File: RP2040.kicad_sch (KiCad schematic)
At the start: 24 parts, among them J1 Conn_01x02, U3 W25Q128JVS, U5 RP2040, Y1 ABM8-272-T3

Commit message: layout rp2040 mwe
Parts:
- J1: now not fitted
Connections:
- no-connect marks 0 -> 1
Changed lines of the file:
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@@
+	)
+	(junction
+		(at 251.46 110.49)
+		(diameter 0)
+		(color 0 0 0 0)
 	)
 	(junction
@@
 	)
 	(junction
-		(at 251.46 110.49)
-		(diameter 0)
-		(color 0 0 0 0)
-	)
-	(junction
 		(at 114.3 194.31)
 		(diameter 0)
 		(color 0 0 0 0)
+	)
+	(no_connect
+		(at 215.9 194.31)
 	)
 	(wire
@@
 				(path "/e63e39d7-6ac0-4ffd-8aa3-1841a4541b55/9c0a3f13-1184-404b-a0f0-9ed0da42fa30"
 					(reference "C7")
-					(unit 1)
-				)
-			)
-		)
-	)
-	(symbol
-		(lib_id "power:+3V3")
-		(at 251.46 110.49 0)
-		(unit 1)
-		(exclude_from_sim no)
-		(in_bom yes)
-		(on_board yes)
-		(dnp no)
-		(property "Reference" "#PWR034"
-			(at 251.46 114.3 0)
-			(effects
-				(font
-					(size 1.27 1.27)
-				)
-				(hide yes)
-			)
-		)
-		(property "Value" "+3V3"
-			(at 251.46 105.41 0)
-			(effects
-				(font
-					(size 1.27 1.27)
-				)
-			)
-		)
-		(property "Footprint" ""
-			(at 251.46 110.49 0)
-			(effects
-				(font
-					(size 1.27 1.27)
-				)
-				(hide yes)
-			)
-		)
-		(property "Datasheet" ""
-			(at 251.46 110.49 0)
-			(effects
-				(font
-					(size 1.27 1.27)
-				)
-				(hide yes)
-			)
-		)
-		(property "Description" ""
-			(at 251.46 110.49 0)
-			(effects
-				(font
-					(size 1.27 1.27)
-				)
-				(hide yes)
-			)
-		)
-		(pin "1"
-		)
-		(instances
-			(project "not-so-fullsize-ortho"
-				(path "/e63e39d7-6ac0-4ffd-8aa3-1841a4541b55/9c0a3f13-1184-404b-a0f0-9ed0da42fa30"
-					(reference "#PWR034")
 					(unit 1)
 				)
@@
 	(symbol
 		(lib_id "power:+3V3")
+		(at 251.46 110.49 0)
+		(unit 1)
+		(exclude_from_sim no)
+		(in_bom yes)
+		(on_board yes)
+		(dnp no)
+		(property "Reference" "#PWR018"
+			(at 251.46 114.3 0)
+			(effects
+				(font
+					(size 1.27 1.27)
+				)
+				(hide yes)
+			)
+		)
+		(property "Value" "+3V3"
+			(at 251.841 106.0958 0)
+			(effects
+				(font
+					(size 1.27 1.27)
+				)
+			)
+		)
+		(property "Footprint" ""
+			(at 251.46 110.49 0)
+			(effects
+				(font
+					(size 1.27 1.27)
+				)
+				(hide yes)
+			)
+		)
+		(property "Datasheet" ""
+			(at 251.46 110.49 0)
+			(effects
+				(font
+					(size 1.27 1.27)
+				)
+				(hide yes)
+			)
+		)
+		(property "Description" ""
+			(at 251.46 110.49 0)
+			(effects
+				(font
+					(size 1.27 1.27)
+				)
+				(hide yes)
+			)
+		)
+		(pin "1"
+		)
+		(instances
+			(project "not-so-fullsize-ortho"
+				(path "/e63e39d7-6ac0-4ffd-8aa3-1841a4541b55/9c0a3f13-1184-404b-a0f0-9ed0da42fa30"
+					(reference "#PWR018")
+					(unit 1)
+				)
+			)
+		)
+	)
+	(symbol
+		(lib_id "power:+3V3")
 		(at 121.92 113.03 0)
 		(unit 1)
@@
 		(in_bom yes)
 		(on_board yes)
-		(dnp no)
+		(dnp yes)
 		(property "Reference" "J1"
 			(at 49.53 134.62 0)

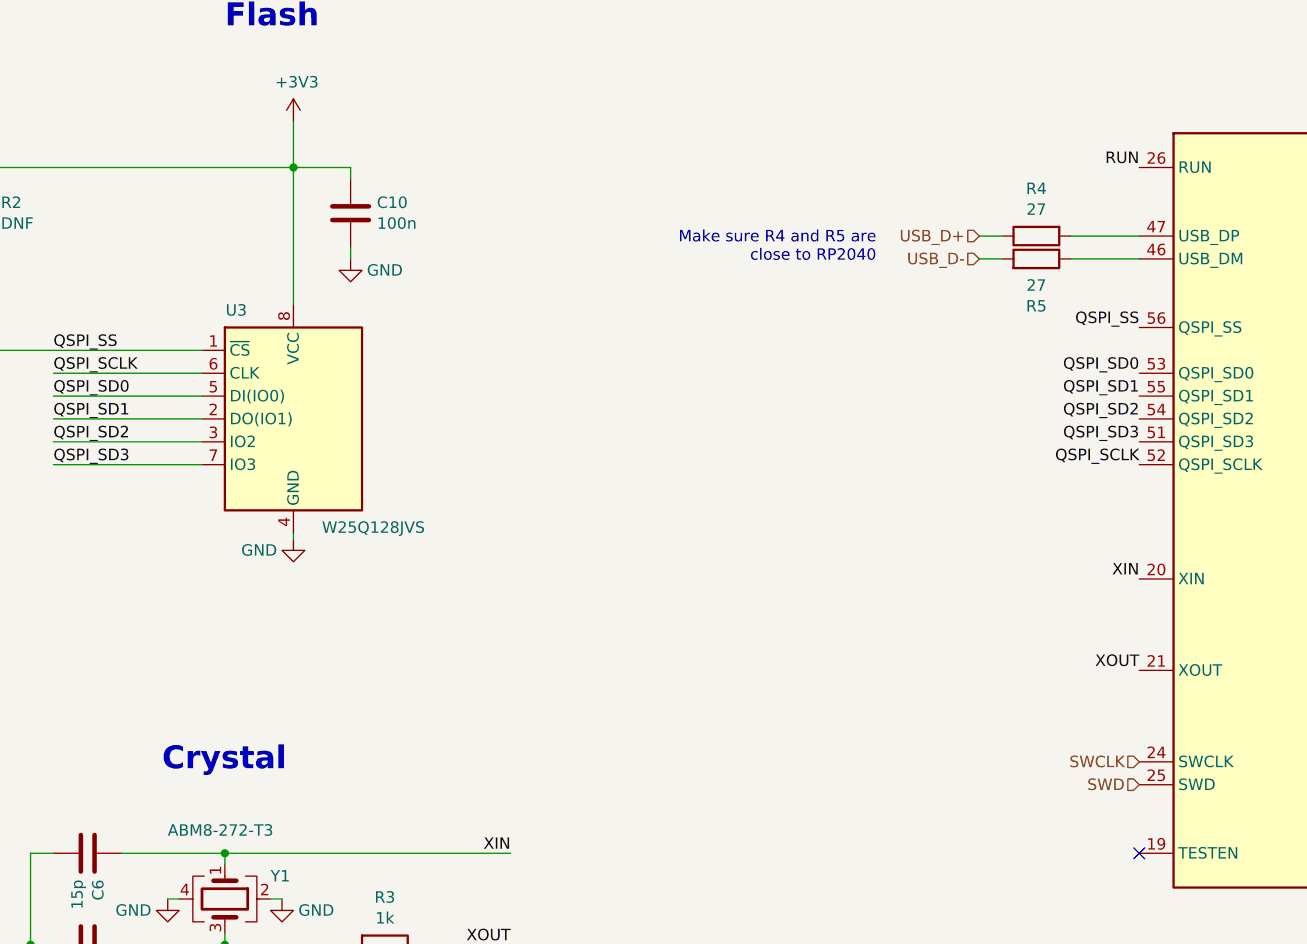
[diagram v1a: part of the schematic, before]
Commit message: routing, rotate leds to make tracks easier
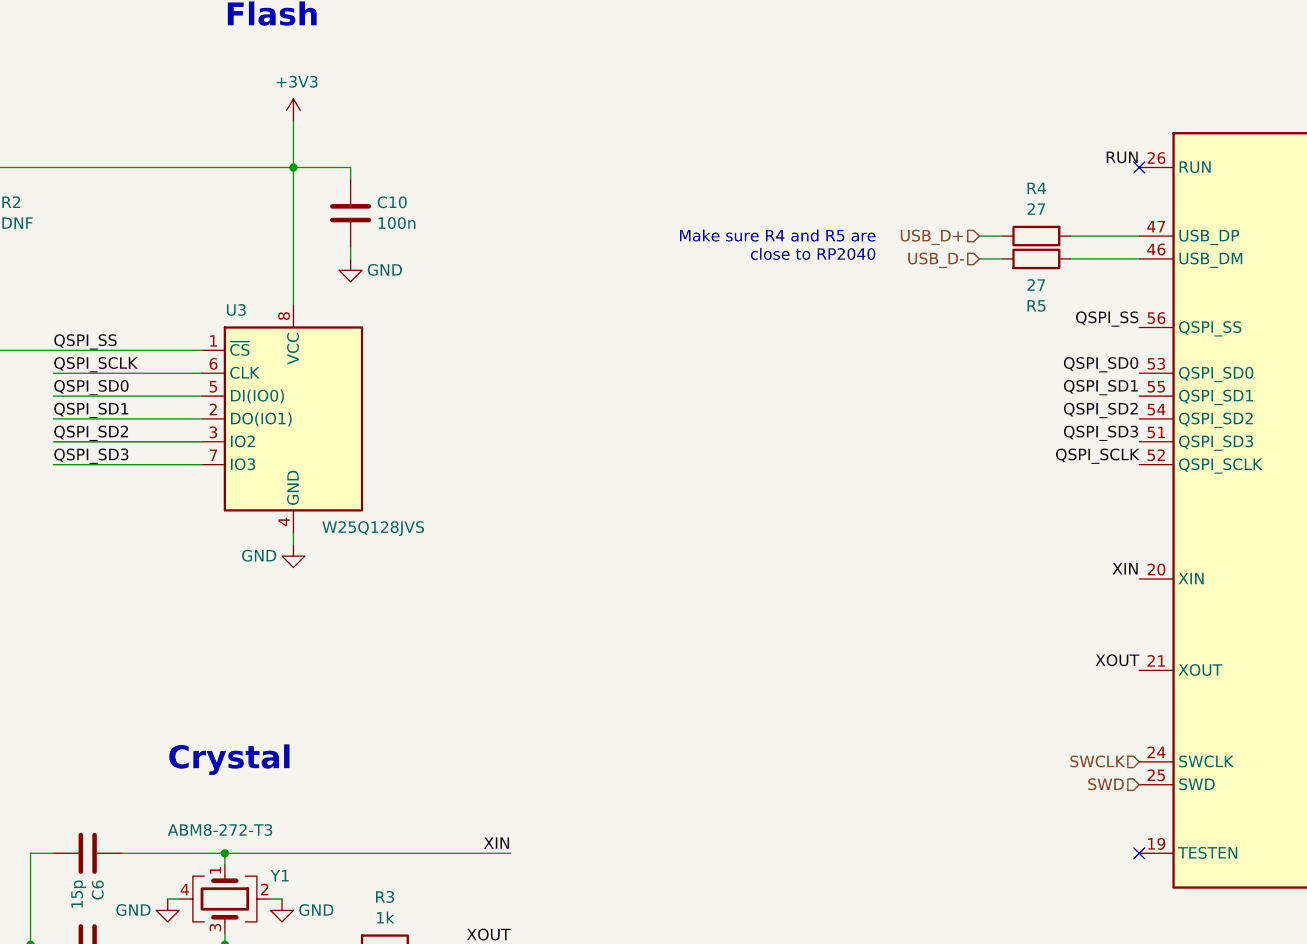
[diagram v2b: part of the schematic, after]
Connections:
- no-connect marks 1 -> 2
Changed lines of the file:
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@@
 		(at 215.9 194.31)
 	)
+	(no_connect
+		(at 215.9 118.11)
+	)
 	(wire
 		(pts
@@
 	(wire
 		(pts
-			(xy 121.92 159.385) (xy 121.92 158.75)
+			(xy 121.92 160.02) (xy 121.92 158.75)
 		)
 		(stroke
@@
 	(text "Crystal"
 		(exclude_from_sim no)
-		(at 107.315 185.42 0)
+		(at 107.95 185.42 0)
 		(effects
 			(font
@@
 			)
 		)
-		(property "Description" ""
+		(property "Description" "Power symbol creates a global label with name \"GND\" , ground"
 			(at 57.15 142.24 0)
 			(effects
@@
 			)
 		)
-		(property "Description" ""
+		(property "Description" "Power symbol creates a global label with name \"+3V3\""
 			(at 389.89 57.15 0)
 			(effects
@@
 			)
 		)
-		(property "Description" ""
+		(property "Description" "Power symbol creates a global label with name \"GND\" , ground"
 			(at 304.8 39.37 0)
 			(effects
@@
 			)
 		)
-		(property "Description" ""
+		(property "Description" "Power symbol creates a global label with name \"+1V1\""
 			(at 332.74 29.21 0)
 			(effects
@@
 			)
 		)
-		(property "Description" ""
+		(property "Description" "Power symbol creates a global label with name \"GND\" , ground"
 			(at 332.74 40.64 0)
 			(effects
@@
 			)
 		)
-		(property "Description" ""
+		(property "Description" "Power symbol creates a global label with name \"+3V3\""
 			(at 251.46 110.49 0)
 			(effects
@@
 			)
 		)
-		(property "Description" ""
+		(property "Description" "Power symbol creates a global label with name \"+3V3\""
 			(at 121.92 113.03 0)
 			(effects
@@
 			)
 		)
-		(property "Description" ""
+		(property "Description" "Power symbol creates a global label with name \"GND\" , ground"
 			(at 107.95 199.39 0)
 			(effects
@@
 			)
 		)
-		(property "Description" ""
+		(property "Description" "Power symbol creates a global label with name \"GND\" , ground"
 			(at 389.89 71.12 0)
 			(effects
@@
 			)
 		)
-		(property "Description" ""
+		(property "Description" "Power symbol creates a global label with name \"GND\" , ground"
 			(at 304.8 68.58 0)
 			(effects
@@
 	(symbol
 		(lib_id "power:GND")
-		(at 121.92 159.385 0)
+		(at 121.92 160.02 0)
 		(unit 1)
 		(exclude_from_sim no)
@@
 		(dnp no)
 		(property "Reference" "#PWR013"
-			(at 121.92 165.735 0)
+			(at 121.92 166.37 0)
 			(effects
 				(font
@@
 		)
 		(property "Value" "GND"
-			(at 118.11 160.655 0)
+			(at 118.11 161.29 0)
 			(effects
 				(font
@@
 		)
 		(property "Footprint" ""
-			(at 121.92 159.385 0)
+			(at 121.92 160.02 0)
 			(effects
 				(font
@@
 		)
 		(property "Datasheet" ""
-			(at 121.92 159.385 0)
+			(at 121.92 160.02 0)
 			(effects
 				(font
@@
 			)
 		)
-		(property "Description" ""
-			(at 121.92 159.385 0)
+		(property "Description" "Power symbol creates a global label with name \"GND\" , ground"
+			(at 121.92 160.02 0)
 			(effects
 				(font
@@
 			)
 		)
-		(property "Description" ""
+		(property "Description" "Power symbol creates a global label with name \"GND\" , ground"
 			(at 389.89 102.87 0)
 			(effects
@@
 			)
 		)
-		(property "Description" ""
+		(property "Description" "Power symbol creates a global label with name \"GND\" , ground"
 			(at 92.71 207.01 0)
 			(effects
@@
 			)
 		)
-		(property "Description" ""
+		(property "Description" "Power symbol creates a global label with name \"+3V3\""
 			(at 389.89 91.44 0)
 			(effects
@@
 			)
 		)
-		(property "Description" ""
+		(property "Description" "Power symbol creates a global label with name \"GND\" , ground"
 			(at 128.27 128.27 0)
 			(effects
@@
 			)
 		)
-		(property "Description" ""
+		(property "Description" "Power symbol creates a global label with name \"GND\" , ground"
 			(at 120.65 199.39 0)
 			(effects
@@
 			)
 		)
-		(property "Description" ""
+		(property "Description" "Power symbol creates a global label with name \"GND\" , ground"
 			(at 241.3 201.93 0)
 			(effects
@@
 			)
 		)
-		(property "Description" ""
+		(property "Description" "Power symbol creates a global label with name \"+1V1\""
 			(at 238.76 110.49 0)
 			(effects

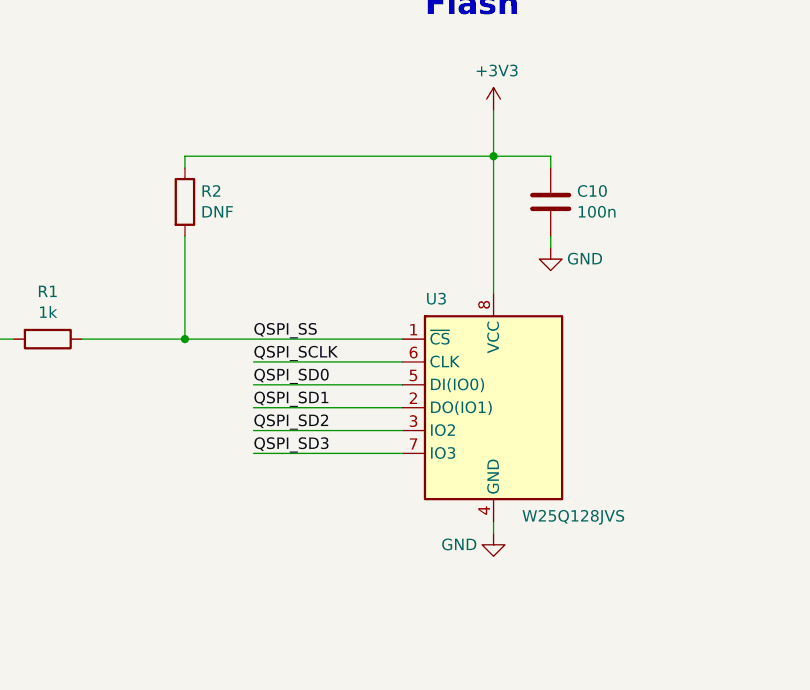
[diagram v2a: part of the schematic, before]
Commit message: add part nums for bom
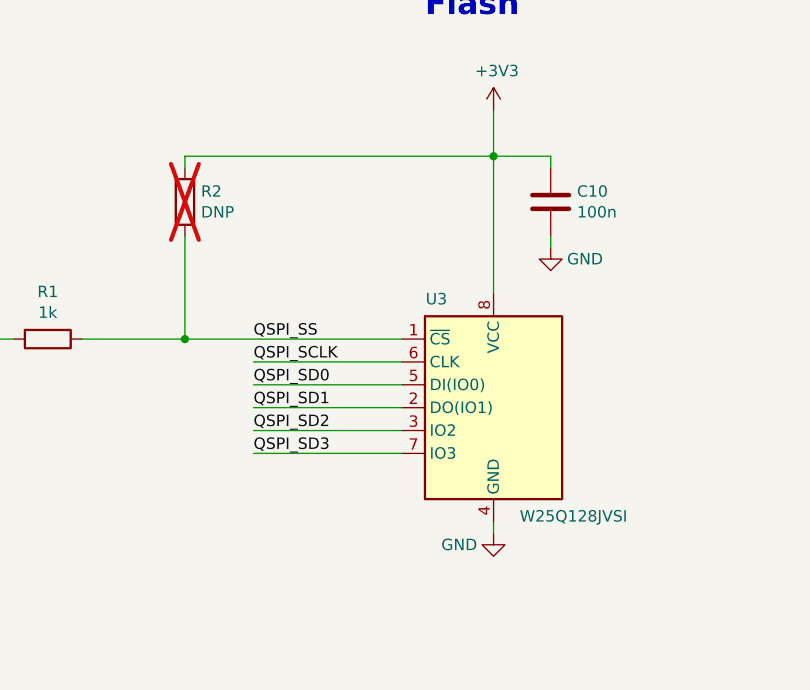
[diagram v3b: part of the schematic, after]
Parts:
- C10, C11, C12, C14, C16, C17, C18, C19, C20, C21: LCSC (none) -> C1525; MPN (none) -> CL05B104KO5NNNC; Manufacturer (none) -> Samsung Electro-Mechanics; Type (none) -> SMD
- C13, C15: LCSC (none) -> C14445; MPN (none) -> CL05A105KP5NNNC; Manufacturer (none) -> Samsung Electro-Mechanics; Type (none) -> SMD
- C22: LCSC (none) -> C15850; MPN (none) -> CL21A106KAYNNNE; Manufacturer (none) -> Samsung Electro-Mechanics; Type (none) -> SMD
- C6, C7: LCSC (none) -> C86285; MPN (none) -> CL05C150JB5NNNC; Manufacturer (none) -> Samsung Electro-Mechanics; Type (none) -> SMD
- J1: Type (none) -> DNS
- R1, R3: LCSC (none) -> C11702; MPN (none) -> 0402WGF1001TCE; Manufacturer (none) -> UNIROYAL; Type (none) -> SMD
- R2: value DNF -> DNP; Type (none) -> DNS; now not fitted
- R4, R5: LCSC (none) -> C25156; MPN (none) -> 0402WGJ0270TCE; Manufacturer (none) -> UNIROYAL; Type (none) -> SMD
- U3: value W25Q128JVS -> W25Q128JVSI; Comment (none) -> Do Not Substitute; LCSC (none) -> C97521; MPN (none) -> W25Q128JVSIQ; Manufacturer (none) -> Winbond Elec; Type (none) -> SMD
- U5: Comment (none) -> Do Not Substitute; LCSC (none) -> C2040; MPN (none) -> RP2040; Manufacturer (none) -> Raspberry Pi Foundation; Type (none) -> SMD
- Y1: Comment (none) -> Do Not Substitute; LCSC (none) -> C20625731; MPN (none) -> ABM8-272-T3; Manufacturer (none) -> Abracon LLC; Type (none) -> SMD

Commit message: usb changes for high power (leds)
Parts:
- renumbered C17 to C51, C12 to C56, C13 to C57, C15 to C58, C20 to C59, C19 to C60, C21 to C63, C16 to C71, C14 to C72, C18 to C73, C10 to C74, C6 to C75, C7 to C76, C11 to C77, C22 to C78, R1 to R6, R2 to R7, R3 to R9, U5 to U4
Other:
- title: (none) -> Raspberry Pi Pico RP2040 MCU Circuit
- moved on the sheet: C51, C56, C57, C58, C59, C60, C63, C71, C72, C73, C74, C75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
